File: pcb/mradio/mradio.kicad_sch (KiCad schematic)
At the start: 40 parts, among them U1 STM32H745ZITx

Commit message: Update some footprints
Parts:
- D1, D2, D3, D4, D5, D6, D7, D8: footprint (none) -> LED_SMD:LED_0603_1608Metric
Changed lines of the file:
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@@
 			)
 		)
-		(property "Footprint" ""
+		(property "Footprint" "LED_SMD:LED_0603_1608Metric"
 			(at 276.86 64.77 0)
 			(hide yes)
@@
 			)
 		)
-		(property "Footprint" ""
+		(property "Footprint" "LED_SMD:LED_0603_1608Metric"
 			(at 276.86 99.06 0)
 			(hide yes)
@@
 			)
 		)
-		(property "Footprint" ""
+		(property "Footprint" "LED_SMD:LED_0603_1608Metric"
 			(at 276.86 87.63 0)
 			(hide yes)
@@
 			)
 		)
-		(property "Footprint" ""
+		(property "Footprint" "LED_SMD:LED_0603_1608Metric"
 			(at 276.86 20.32 0)
 			(hide yes)
@@
 			)
 		)
-		(property "Footprint" ""
+		(property "Footprint" "LED_SMD:LED_0603_1608Metric"
 			(at 276.86 43.18 0)
 			(hide yes)
@@
 			)
 		)
-		(property "Footprint" ""
+		(property "Footprint" "LED_SMD:LED_0603_1608Metric"
 			(at 276.86 31.75 0)
 			(hide yes)
@@
 			)
 		)
-		(property "Footprint" ""
+		(property "Footprint" "LED_SMD:LED_0603_1608Metric"
 			(at 276.86 54.61 0)
 			(hide yes)
@@
 			)
 		)
-		(property "Footprint" ""
+		(property "Footprint" "LED_SMD:LED_0603_1608Metric"
 			(at 276.86 76.2 0)
 			(hide yes)

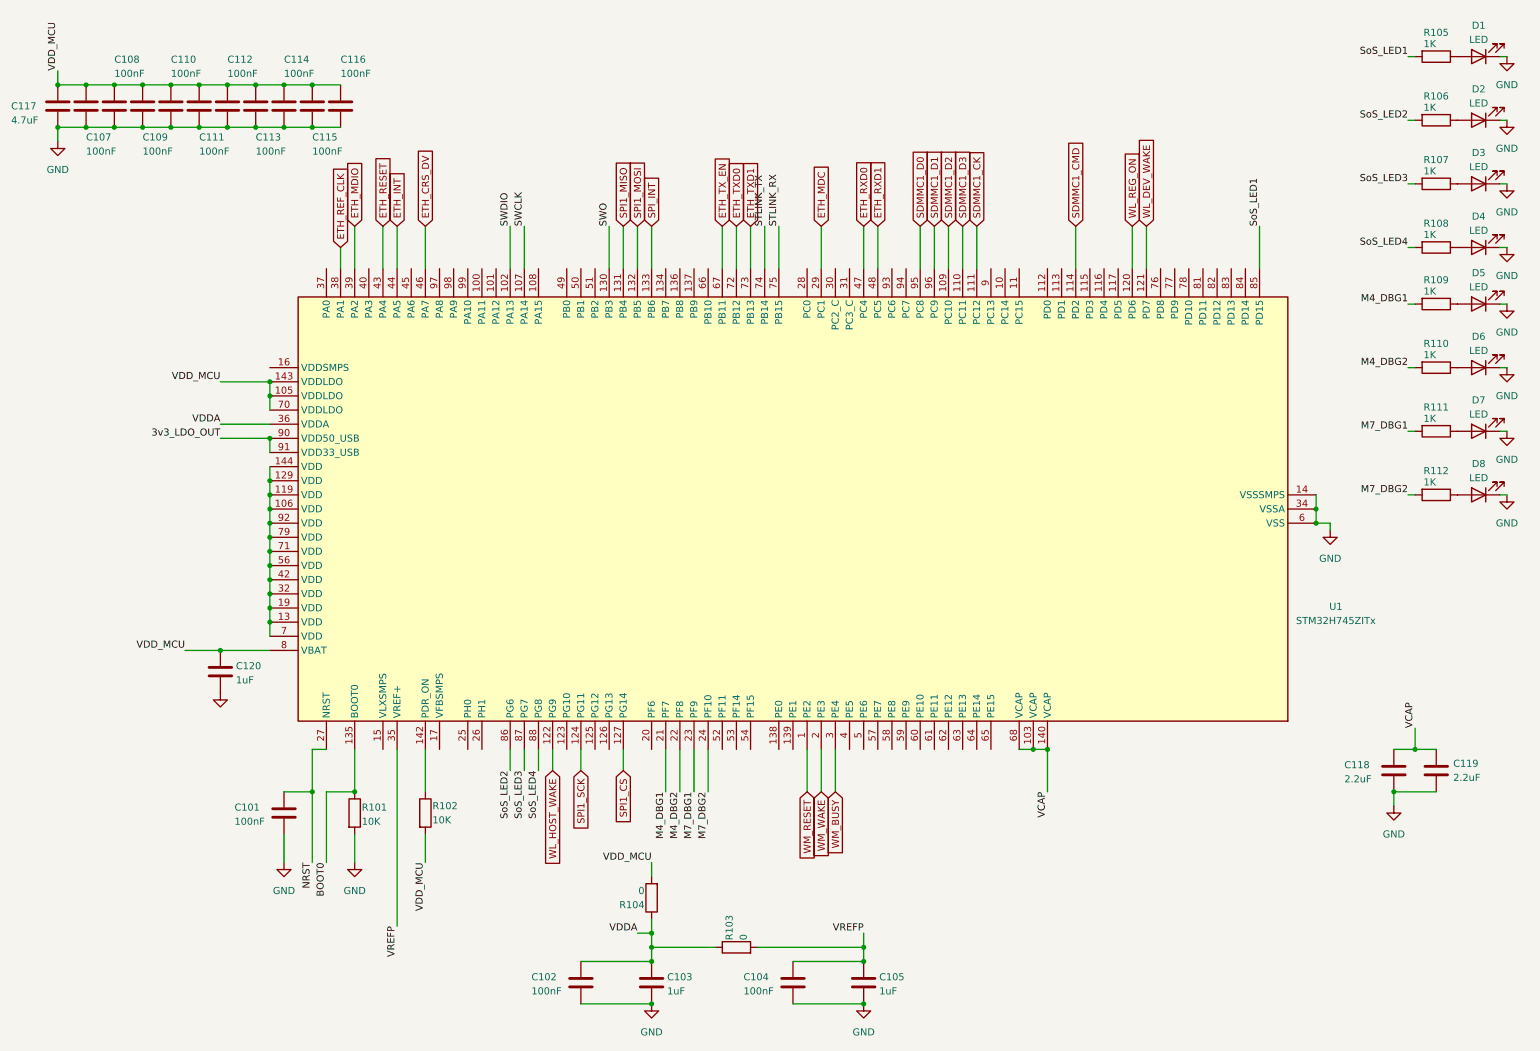
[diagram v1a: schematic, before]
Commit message: updated mcu schematic to support 1.8V
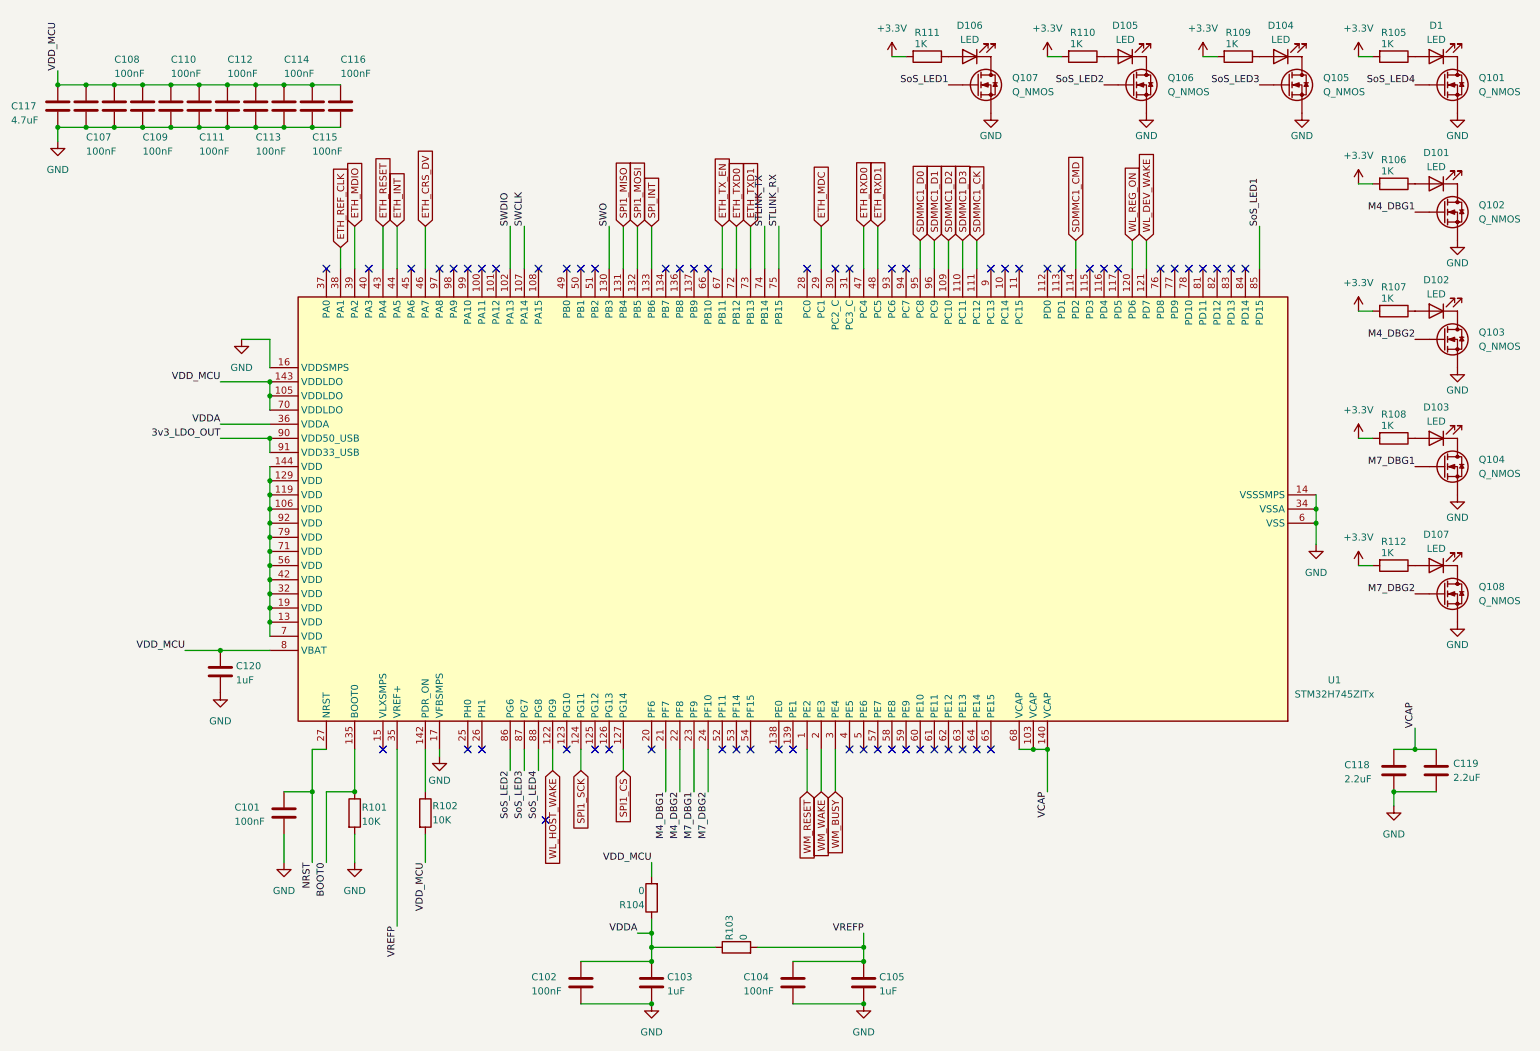
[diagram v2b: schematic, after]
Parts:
- removed D2, D3, D4, D5, D6, D7, D8: LED, LED_SMD:LED_0603_1608Metric, symbol Device:LED
- added D101, D102, D103, D104, D105, D106, D107: LED, LED_SMD:LED_0603_1608Metric, symbol Device:LED
- added Q101, Q102, Q103, Q104, Q105, Q106, Q107, Q108: Q_NMOS, Package_QFP:TQFP-44_10x10mm_P0.8mm, symbol Device:Q_NMOS
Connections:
- net GND: now also U1.16 (VDDSMPS), U1.17 (VFBSMPS), Q101.S, Q102.S, Q103.S, Q104.S, Q105.S, Q106.S, Q107.S, Q108.S; no longer D1.1 (K)
- net M4_DBG1: now also Q102.G; no longer R109.2
- net M4_DBG2: now also Q103.G; no longer R110.2
- net M7_DBG1: now also Q104.G; no longer R111.2
- net M7_DBG2: now also Q108.G; no longer R112.2
- net SoS_LED1: now also Q107.G; no longer R105.2
- net SoS_LED2: now also Q106.G; no longer R106.2
- net SoS_LED3: now also Q105.G; no longer R107.2
- net SoS_LED4: now also Q101.G; no longer R108.2
- net at R109.1: now also D104.2 (A)
- net at R112.1: now also D107.2 (A)
- net at R111.1: now also D106.2 (A)
- net at R107.1: now also D102.2 (A)
- net at R106.1: now also D101.2 (A)
- net at R108.1: now also D103.2 (A)
- net at R110.1: now also D105.2 (A)
- new net: D106.1 (K), Q107.D
- new net: D104.1 (K), Q105.D
- new net: D107.1 (K), Q108.D
- new net: D102.1 (K), Q103.D
- new net: D1.1 (K), Q101.D
- new net: D105.1 (K), Q106.D
- new net: D101.1 (K), Q102.D
- new net: D103.1 (K), Q104.D
- new net +3.3V: R105.2, R106.2, R107.2, R108.2, R109.2, R110.2, R111.2, R112.2
- no-connect marks 0 -> 60
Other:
- moved on the sheet: D1, R105

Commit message: fixed erc errors
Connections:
- net +3.3V is gone; now on net 3v3_LDO_OUT: R105.2, R106.2, R107.2, R108.2, R109.2, R110.2, R111.2, R112.2
- net VDD_MCU: now also U1.106 (VDD), U1.119 (VDD), U1.129 (VDD), U1.13 (VDD), U1.144 (VDD), U1.19 (VDD), U1.32 (VDD), U1.42 (VDD), U1.56 (VDD), U1.7 (VDD), U1.71 (VDD), U1.79 (VDD), U1.92 (VDD)
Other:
- moved on the sheet: D1, D104, D105, D106, Q101, Q105, Q106, Q107, R105, R109, R110, R111

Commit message: mcu vdd fixed
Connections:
- net 3v3_LDO_OUT renamed +3V3
- net VDD_MCU renamed +1V8
- no-connect marks 60 -> 59

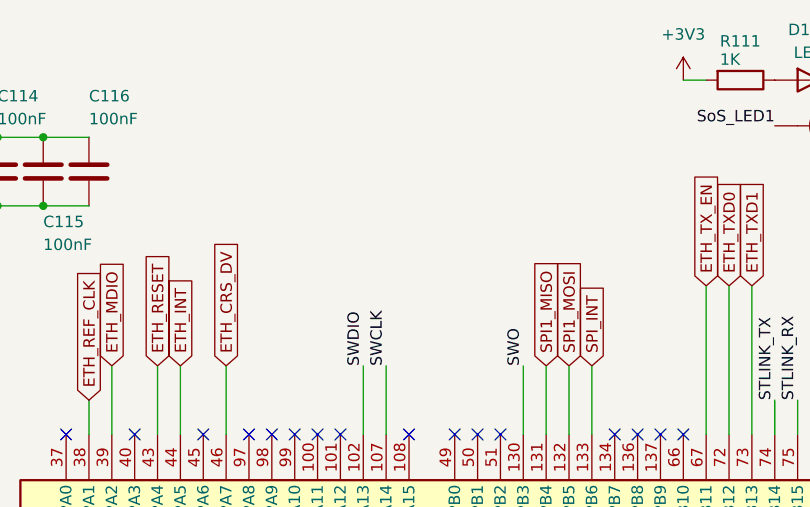
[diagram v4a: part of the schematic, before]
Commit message: Add flashing header
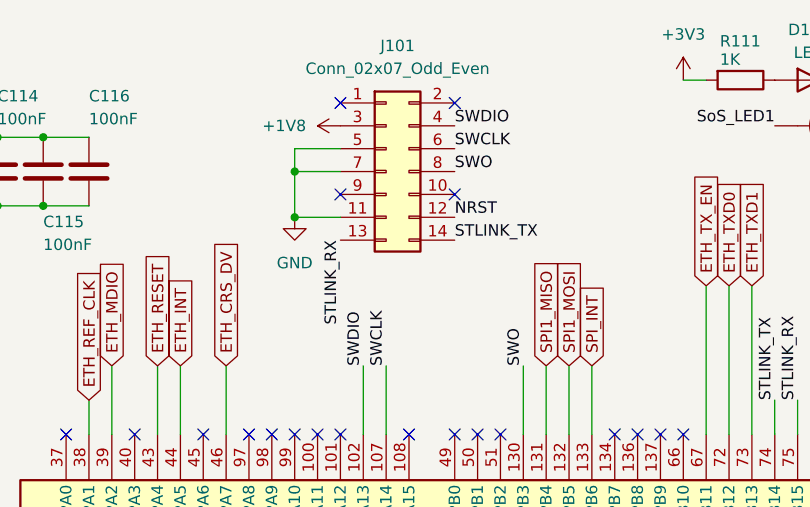
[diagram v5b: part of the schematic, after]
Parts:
- added J101: Conn_02x07_Odd_Even, FTSH-107:SAMTEC_FTSH-107-01-X-DV-K, symbol Connector_Generic:Conn_02x07_Odd_Even
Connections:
- net +1V8: now also J101.3 (Pin_3)
- net GND: now also J101.11 (Pin_11), J101.5 (Pin_5), J101.7 (Pin_7)
- net NRST: now also J101.12 (Pin_12)
- net STLINK_RX: now also J101.13 (Pin_13)
- net STLINK_TX: now also J101.14 (Pin_14)
- net SWCLK: now also J101.6 (Pin_6)
- net SWDIO: now also J101.4 (Pin_4)
- net SWO: now also J101.8 (Pin_8)
- no-connect marks 59 -> 63

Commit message: fix fet footprints
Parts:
- Q101, Q102, Q103, Q104, Q105, Q106, Q107, Q108: footprint Package_QFP:TQFP-44_10x10mm_P0.8mm -> SSM3K56FS:SSM_TOS
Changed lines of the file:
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@@
 			)
 		)
-		(property "Footprint" "Package_QFP:TQFP-44_10x10mm_P0.8mm"
+		(property "Footprint" "SSM3K56FS:SSM_TOS"
 			(at 237.49 21.59 0)
 			(hide yes)
@@
 			)
 		)
-		(property "Footprint" "Package_QFP:TQFP-44_10x10mm_P0.8mm"
+		(property "Footprint" "SSM3K56FS:SSM_TOS"
 			(at 275.59 68.58 0)
 			(hide yes)
@@
 			)
 		)
-		(property "Footprint" "Package_QFP:TQFP-44_10x10mm_P0.8mm"
+		(property "Footprint" "SSM3K56FS:SSM_TOS"
 			(at 158.75 21.59 0)
 			(hide yes)
@@
 			)
 		)
-		(property "Footprint" "Package_QFP:TQFP-44_10x10mm_P0.8mm"
+		(property "Footprint" "SSM3K56FS:SSM_TOS"
 			(at 198.12 21.59 0)
 			(hide yes)
@@
 			)
 		)
-		(property "Footprint" "Package_QFP:TQFP-44_10x10mm_P0.8mm"
+		(property "Footprint" "SSM3K56FS:SSM_TOS"
 			(at 275.59 45.72 0)
 			(hide yes)
@@
 			)
 		)
-		(property "Footprint" "Package_QFP:TQFP-44_10x10mm_P0.8mm"
+		(property "Footprint" "SSM3K56FS:SSM_TOS"
 			(at 275.59 91.44 0)
 			(hide yes)
@@
 			)
 		)
-		(property "Footprint" "Package_QFP:TQFP-44_10x10mm_P0.8mm"
+		(property "Footprint" "SSM3K56FS:SSM_TOS"
 			(at 275.59 21.59 0)
 			(hide yes)
@@
 			)
 		)
-		(property "Footprint" "Package_QFP:TQFP-44_10x10mm_P0.8mm"
+		(property "Footprint" "SSM3K56FS:SSM_TOS"
 			(at 275.59 114.3 0)
 			(hide yes)

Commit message: Fix footprints
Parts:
- Q101, Q102, Q103, Q104, Q105, Q106, Q107, Q108: footprint SSM3K56FS:SSM_TOS -> SSM3K56FS:SSM_TOS_REAL
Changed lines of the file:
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@@
 			)
 		)
-		(property "Footprint" "SSM3K56FS:SSM_TOS"
+		(property "Footprint" "SSM3K56FS:SSM_TOS_REAL"
 			(at 237.49 21.59 0)
 			(hide yes)
@@
 			)
 		)
-		(property "Footprint" "SSM3K56FS:SSM_TOS"
+		(property "Footprint" "SSM3K56FS:SSM_TOS_REAL"
 			(at 275.59 68.58 0)
 			(hide yes)
@@
 			)
 		)
-		(property "Footprint" "SSM3K56FS:SSM_TOS"
+		(property "Footprint" "SSM3K56FS:SSM_TOS_REAL"
 			(at 158.75 21.59 0)
 			(hide yes)
@@
 			)
 		)
-		(property "Footprint" "SSM3K56FS:SSM_TOS"
+		(property "Footprint" "SSM3K56FS:SSM_TOS_REAL"
 			(at 198.12 21.59 0)
 			(hide yes)
@@
 			)
 		)
-		(property "Footprint" "SSM3K56FS:SSM_TOS"
+		(property "Footprint" "SSM3K56FS:SSM_TOS_REAL"
 			(at 275.59 45.72 0)
 			(hide yes)
@@
 			)
 		)
-		(property "Footprint" "SSM3K56FS:SSM_TOS"
+		(property "Footprint" "SSM3K56FS:SSM_TOS_REAL"
 			(at 275.59 91.44 0)
 			(hide yes)
@@
 			)
 		)
-		(property "Footprint" "SSM3K56FS:SSM_TOS"
+		(property "Footprint" "SSM3K56FS:SSM_TOS_REAL"
 			(at 275.59 21.59 0)
 			(hide yes)
@@
 			)
 		)
-		(property "Footprint" "SSM3K56FS:SSM_TOS"
+		(property "Footprint" "SSM3K56FS:SSM_TOS_REAL"
 			(at 275.59 114.3 0)
 			(hide yes)

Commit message: finished component placement
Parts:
- added C106: 4.7uF, Capacitor_SMD:C_0603_1608Metric, symbol Device:C
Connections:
- net +1V8: now also C106.2
- net GND: now also C106.1
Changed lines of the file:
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@@
 	)
 	(junction
+		(at 57.15 78.74)
+		(diameter 0)
+		(color 0 0 0 0)
+	)
+	(junction
 		(at 52.07 25.4)
 		(diameter 0)
@@
 	)
 	(junction
+		(at 57.15 71.12)
+		(diameter 0)
+		(color 0 0 0 0)
+	)
+	(junction
 		(at 31.75 33.02)
 		(diameter 0)
@@
 	(wire
 		(pts
-			(xy 50.8 78.74) (xy 59.69 78.74)
+			(xy 50.8 78.74) (xy 57.15 78.74)
 		)
 		(stroke
@@
 	(wire
 		(pts
-			(xy 54.61 71.12) (xy 59.69 71.12)
+			(xy 57.15 78.74) (xy 59.69 78.74)
+		)
+		(stroke
+			(width 0)
+			(type default)
+		)
+	)
+	(wire
+		(pts
+			(xy 54.61 71.12) (xy 57.15 71.12)
 		)
 		(stroke
@@
 	(wire
 		(pts
+			(xy 57.15 71.12) (xy 59.69 71.12)
+		)
+		(stroke
+			(width 0)
+			(type default)
+		)
+	)
+	(wire
+		(pts
 			(xy 217.17 53.34) (xy 217.17 58.42)
 		)
@@
 		(in_pos_files yes)
 		(dnp no)
-		(fields_autoplaced yes)
 		(property "Reference" "#PWR0104"
 			(at 54.61 77.47 0)
@@
 		)
 		(property "Value" "GND"
-			(at 54.61 76.2 0)
+			(at 50.8 71.628 0)
 			(show_name no)
 			(do_not_autoplace no)
@@
 	(symbol
 		(lib_id "Device:C")
+		(at 57.15 74.93 0)
+		(unit 1)
+		(body_style 1)
+		(exclude_from_sim no)
+		(in_bom yes)
+		(on_board yes)
+		(in_pos_files yes)
+		(dnp no)
+		(property "Reference" "C106"
+			(at 48.768 74.93 0)
+			(show_name no)
+			(do_not_autoplace no)
+			(effects
+				(font
+					(size 1.27 1.27)
+				)
+				(justify left)
+			)
+		)
+		(property "Value" "4.7uF"
+			(at 50.292 77.47 0)
+			(show_name no)
+			(do_not_autoplace no)
+			(effects
+				(font
+					(size 1.27 1.27)
+				)
+				(justify left)
+			)
+		)
+		(property "Footprint" "Capacitor_SMD:C_0603_1608Metric"
+			(at 58.1152 78.74 0)
+			(hide yes)
+			(show_name no)
+			(do_not_autoplace no)
+			(effects
+				(font
+					(size 1.27 1.27)
+				)
+			)
+		)
+		(property "Datasheet" ""
+			(at 57.15 74.93 0)
+			(hide yes)
+			(show_name no)
+			(do_not_autoplace no)
+			(effects
+				(font
+					(size 1.27 1.27)
+				)
+			)
+		)
+		(property "Description" "Unpolarized capacitor"
+			(at 57.15 74.93 0)
+			(hide yes)
+			(show_name no)
+			(do_not_autoplace no)
+			(effects
+				(font
+					(size 1.27 1.27)
+				)
+			)
+		)
+		(pin "1"
+		)
+		(pin "2"
+		)
+		(instances
+			(project "mradio"
+				(path "/8dc7c7b7-3424-46ed-8e13-a2f5eca35b9b"
+					(reference "C106")
+					(unit 1)
+				)
+			)
+		)
+	)
+	(symbol
+		(lib_id "Device:C")
 		(at 26.67 29.21 0)
 		(unit 1)
@@
 		)
 		(property "Value" "PWR_FLAG"
-			(at 53.34 82.296 0)
+			(at 53.594 87.884 0)
 			(show_name no)
 			(do_not_autoplace no)
